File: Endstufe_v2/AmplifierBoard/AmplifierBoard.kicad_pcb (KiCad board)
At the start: 4 copper layers, 125 x 90 mm, 120 parts, among them J1 Conn_01x01_Pin, J10 Conn_02x06_Top_Bottom, J11 B6B-XH-2(LF)(SN), J12 B6B-XH-2(LF)(SN), J13 Conn_01x02_Pin, J14 Conn_01x02_Pin, J15 Conn_01x02_Pin, J16 Conn_01x04, J17 Conn_01x02_Pin, J2 Conn_01x01_Pin, J3 banana connector, J4 banana connector, J5 banana connector, J6 banana connector, J7 banana connector, J8 banana connector, J9 ST-0322D00-071-1A2H, U1 TPA3126D2DADR, U2 TPA3126D2DADR, U3 NVTFWS014P04M8LTAG, U4 1SMA5927A

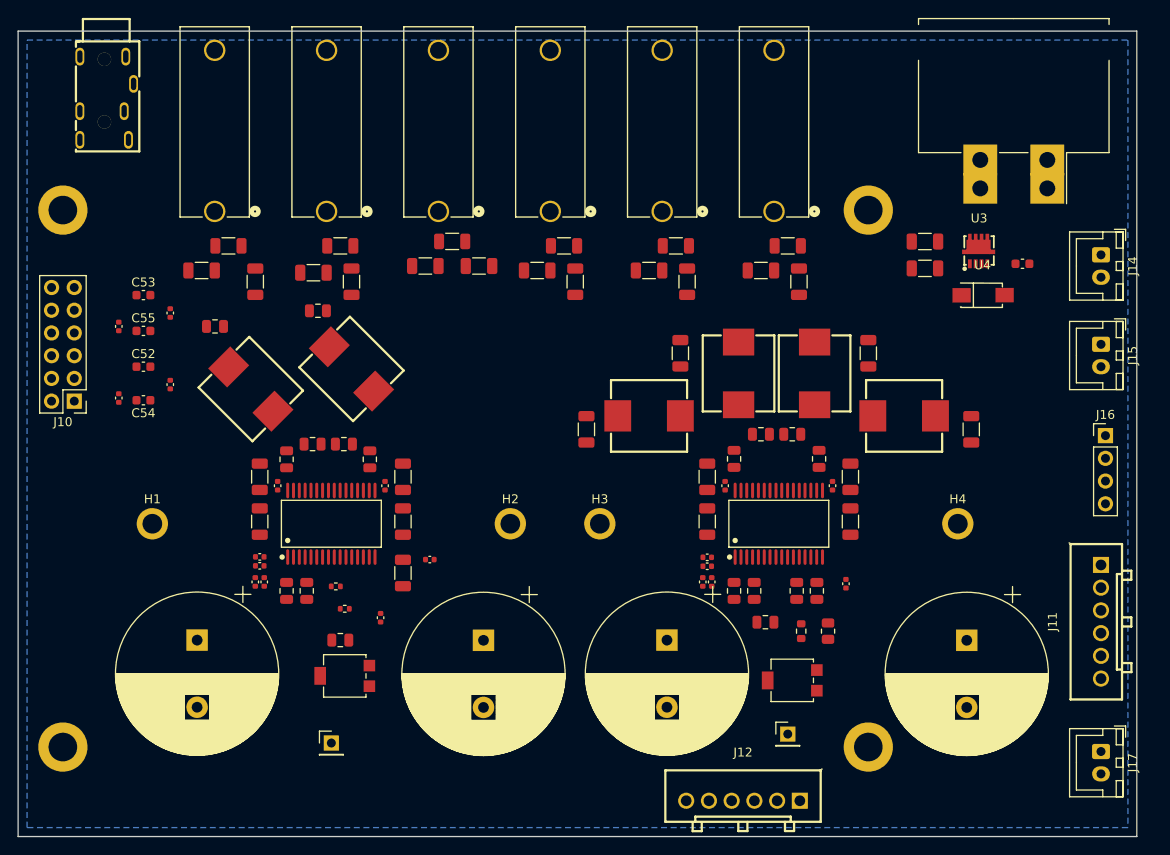
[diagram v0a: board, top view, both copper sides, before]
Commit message: Route Power and Audio Signals
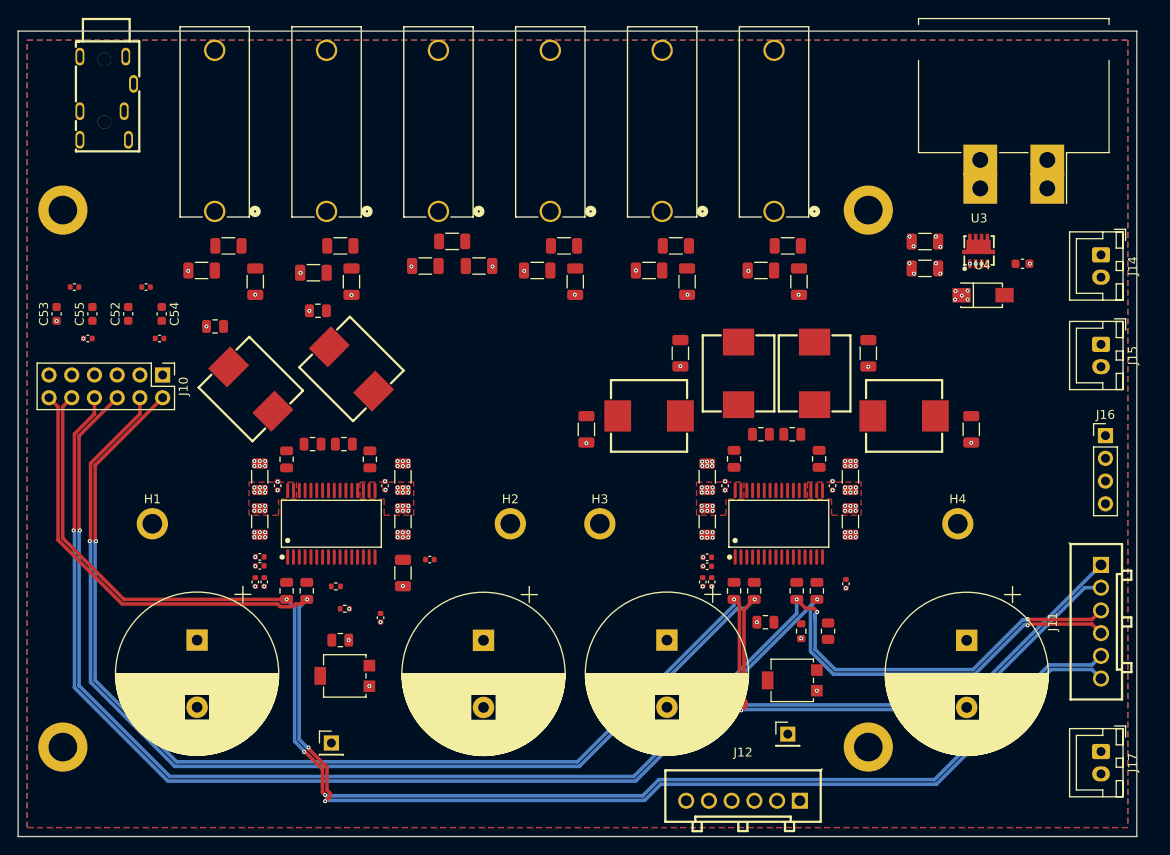
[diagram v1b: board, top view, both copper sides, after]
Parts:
- moved R18 11.2 mm to (149.3, 78.6), turned to 180 degrees
- moved R19 11.1 mm to (141.3, 78.6), turned to 180 degrees
- moved J10 10.3 mm to (151.2, 88.4), turned to -90 degrees
- moved C53 9.92 mm to (139.3, 81.6), turned to 90 degrees
- moved C54 9.87 mm to (151.1, 81.6), turned to -90 degrees
- moved R21 8.06 mm to (150.8, 84.3), turned to 180 degrees
- moved C52 6.14 mm to (147.3, 81.6), turned to 90 degrees
- moved C55 6.01 mm to (143.3, 81.6), turned to 90 degrees
- moved R20 3.70 mm to (142.8, 84.3), turned to 180 degrees
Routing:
- net /TPA3126D2/RINN: track 0.00 -> 179.1 mm, vias 0 -> 3
- net /TPA3126D2/RINP: track 0.00 -> 176.6 mm, vias 0 -> 3
- net /TPA3126D2/LINP: track 0.00 -> 171.0 mm, vias 0 -> 4
- net /TPA3126D2/LINN: track 0.00 -> 170.7 mm, vias 0 -> 3
- net /TPA3126D2/SINN: track 0.00 -> 165.6 mm, vias 0 -> 3
- net /TPA3126D2/SINP: track 0.00 -> 160.9 mm, vias 0 -> 3
- net GND: vias 0 -> 90
- net +24V: vias 0 -> 68
- added copper zone on F.Cu, net +24V
- added copper zone on F.Cu, net GND

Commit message: Route TPA3126D2 output signals
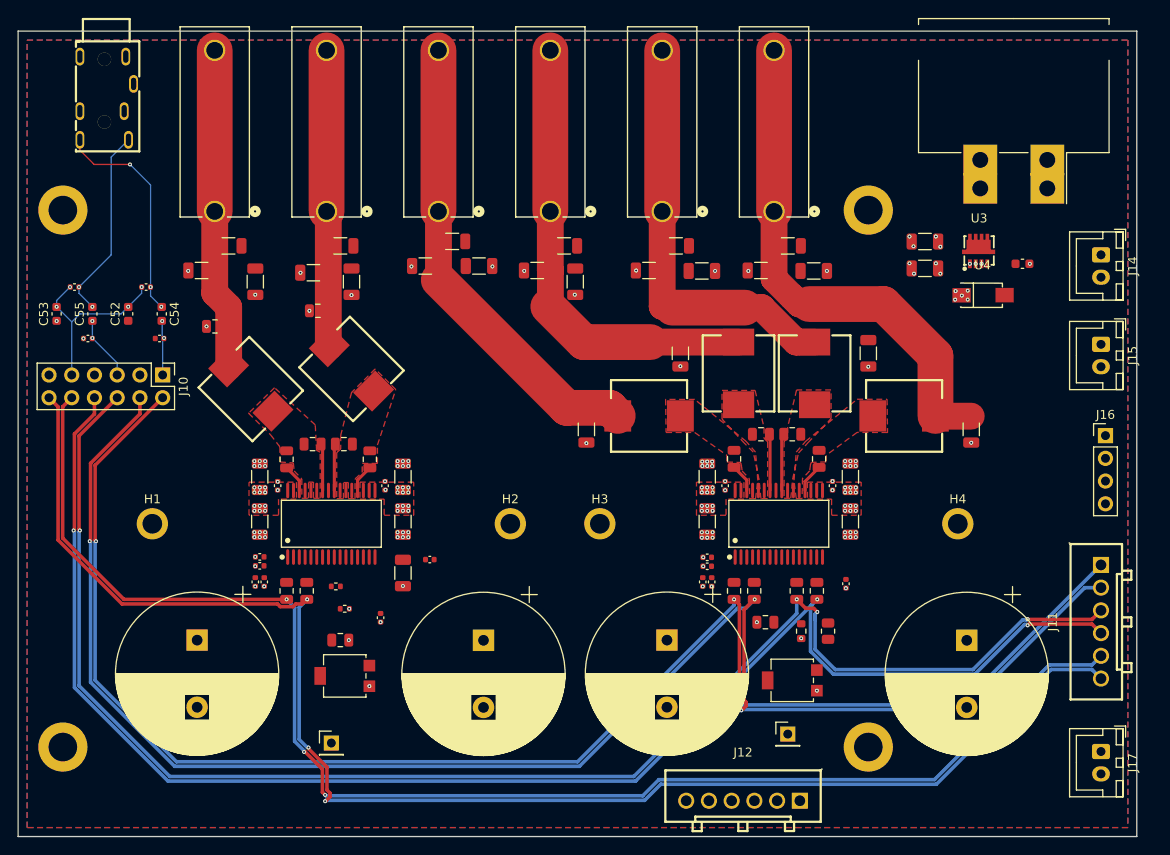
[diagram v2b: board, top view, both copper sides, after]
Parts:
- moved C48 2.04 mm to (211.4, 76.8), turned to 0 degrees
- moved C49 2.04 mm to (223.9, 76.8), turned to 180 degrees
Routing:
- net Net-(J6-Pin_1): track 0.00 -> 57.8 mm
- net Net-(J3-Pin_1): track 0.00 -> 52.0 mm
- net Net-(J4-Pin_1): track 0.00 -> 51.1 mm
- net Net-(J5-Pin_1): track 0.00 -> 47.3 mm
- net Net-(J7-Pin_1): track 0.00 -> 36.0 mm
- net Net-(J8-Pin_1): track 0.00 -> 33.3 mm
- net Net-(J9-AUDIO_R): track 0.00 -> 24.8 mm, vias 0 -> 3
- net Net-(J9-AUDIO_L): track 0.00 -> 21.6 mm, vias 0 -> 2
- net /SIN: track 0.00 -> 21.0 mm, vias 0 -> 4
- net /LIN: track 0.00 -> 7.17 mm, vias 0 -> 2
- net Net-(U1-BSPL): track 0.00 -> 6.37 mm
- net Net-(U1-BSNR): track 0.00 -> 6.31 mm
- net /RIN: track 0.00 -> 6.17 mm, vias 0 -> 2
- net Net-(U2-BSNR): track 0.00 -> 5.25 mm
- net Net-(U2-BSPL): track 0.00 -> 5.23 mm
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- added copper zone on F.Cu, net Net-(U1-OUTNL)
- added copper zone on F.Cu, net Net-(U1-OUTNR)
- added copper zone on F.Cu, net Net-(U1-OUTPL)
- added copper zone on F.Cu, net Net-(U1-OUTPR)
- added copper zone on F.Cu, net Net-(U2-OUTNL)
- added copper zone on F.Cu, net Net-(U2-OUTNR)

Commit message: Finish routing of amplifier board
Signals are now on layer 2, and layer 3 is 24V, layer 4 is GND.
This makes the outer layers solid GND without many heat flow obstacles
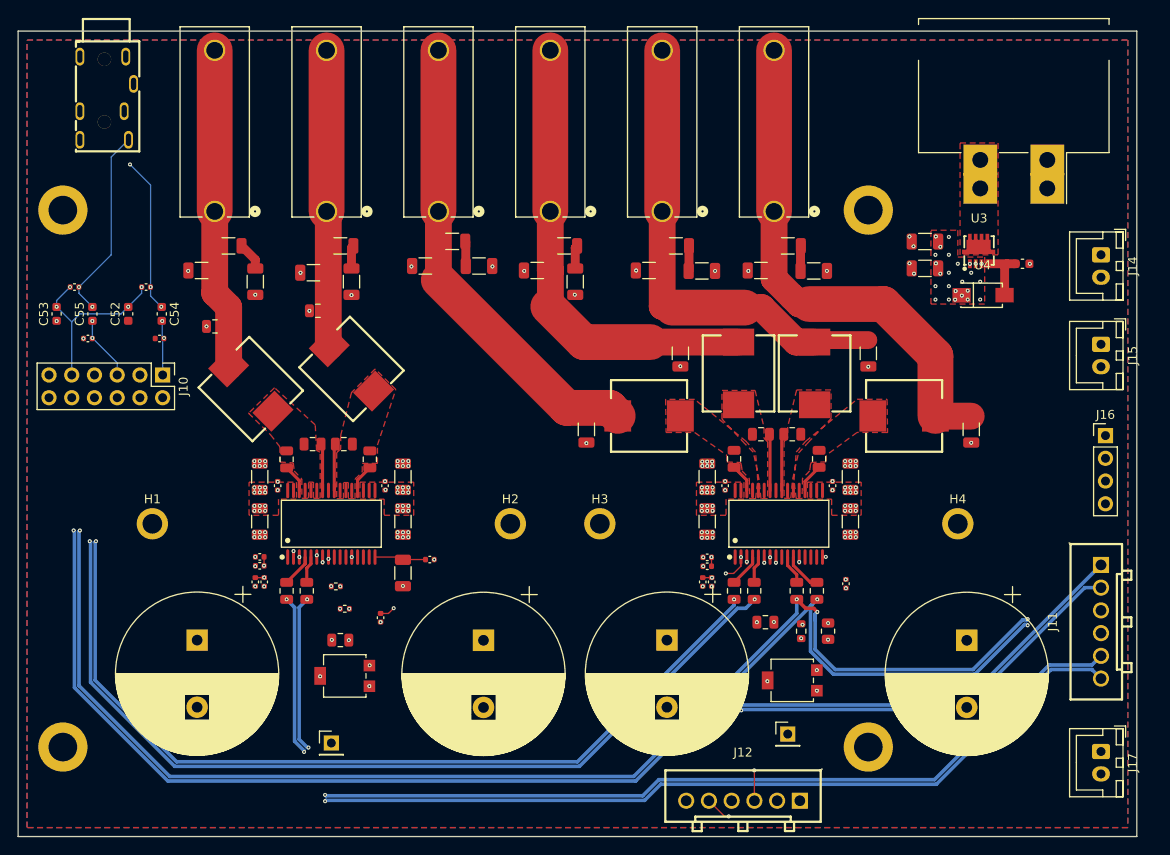
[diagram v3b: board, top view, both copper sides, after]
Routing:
- net /TPA3126D2/SDZB: track 0.00 -> 73.0 mm, vias 0 -> 2
- net /TPA3126D2/FAULTZB: track 0.00 -> 70.4 mm, vias 0 -> 2
- net /TPA3126D2/MUTEB: track 0.00 -> 51.0 mm, vias 0 -> 2
- net /TPA3126D2/SYNC: track 0.00 -> 46.9 mm, vias 0 -> 2
- net /TPA3126D2/MUTEA: track 0.00 -> 46.3 mm, vias 0 -> 3
- net /TPA3126D2/SDZA: track 0.00 -> 36.5 mm, vias 0 -> 3
- net /TPA3126D2/FAULTZA: track 0.00 -> 33.4 mm, vias 0 -> 3
- net Net-(J2-Pin_1): track 0.00 -> 21.6 mm, vias 0 -> 2
- net Net-(J1-Pin_1): track 0.00 -> 20.2 mm, vias 0 -> 2
- net Net-(U1-GVDD): track 0.00 -> 17.5 mm, vias 0 -> 4
- net Net-(U2-GVDD): track 0.00 -> 14.7 mm, vias 0 -> 4
- net Net-(U1-GAIN_SLV): track 0.00 -> 11.1 mm, vias 0 -> 3
- net Net-(U3-G): track 0.00 -> 6.58 mm
- net Net-(U2-GAIN_SLV): track 0.00 -> 6.21 mm, vias 0 -> 3
- net Net-(J5-Pin_1): track 47.3 -> 53.4 mm
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- added copper zone on In2.Cu, net +24V
- added copper zone on B.Cu, net GND
- added copper zone on F.Cu, net Net-(J13-Pin_2)
- removed copper zone on B.Cu, net +24V

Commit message: Make boards compliant with JLCPCB
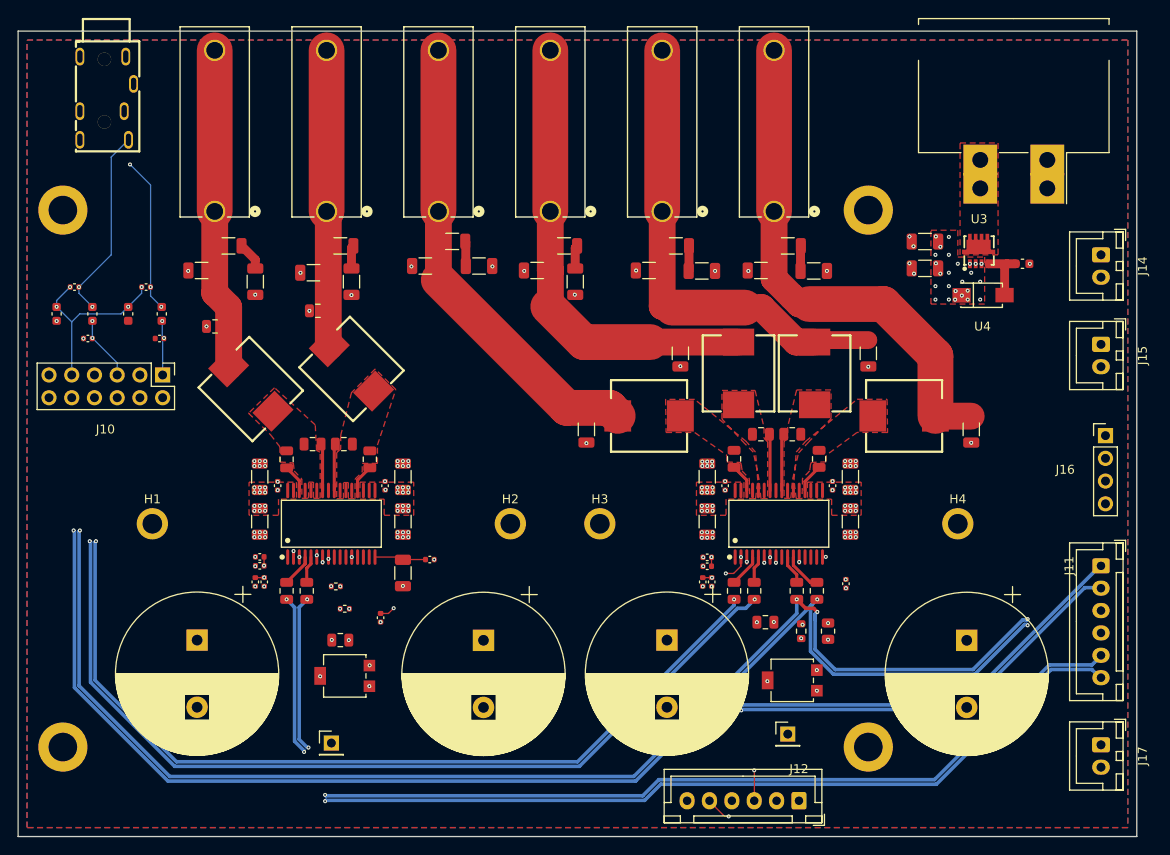
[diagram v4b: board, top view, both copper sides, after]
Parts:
- J10: value Conn_02x06_Top_Bottom -> DNP
- J11, J12: footprint Endstufe:CONN-TH_B6B-XH-2-LF-SN -> Endstufe:JST_XH_B6B-XH-A_1x06_P2.50mm_Vertical
- J13: value Conn_01x02_Pin -> DNP
- J14, J15, J17: footprint Connector_JST:JST_XH_B2B-XH-A_1x02_P2.50mm_Vertical -> Endstufe:JST_XH_B2B-XH-A_1x02_P2.50mm_Vertical
- J16: value Conn_01x04 -> DNP
- moved J14 1.25 mm to (256.0, 76.2), turned to 90 degrees
- moved J15 1.25 mm to (256.0, 86.2), turned to 90 degrees
- moved J17 0.50 mm to (256.0, 131.0), turned to 90 degrees

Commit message: Change unavailable parts to available ones, optimise silkscreen, do via stiching
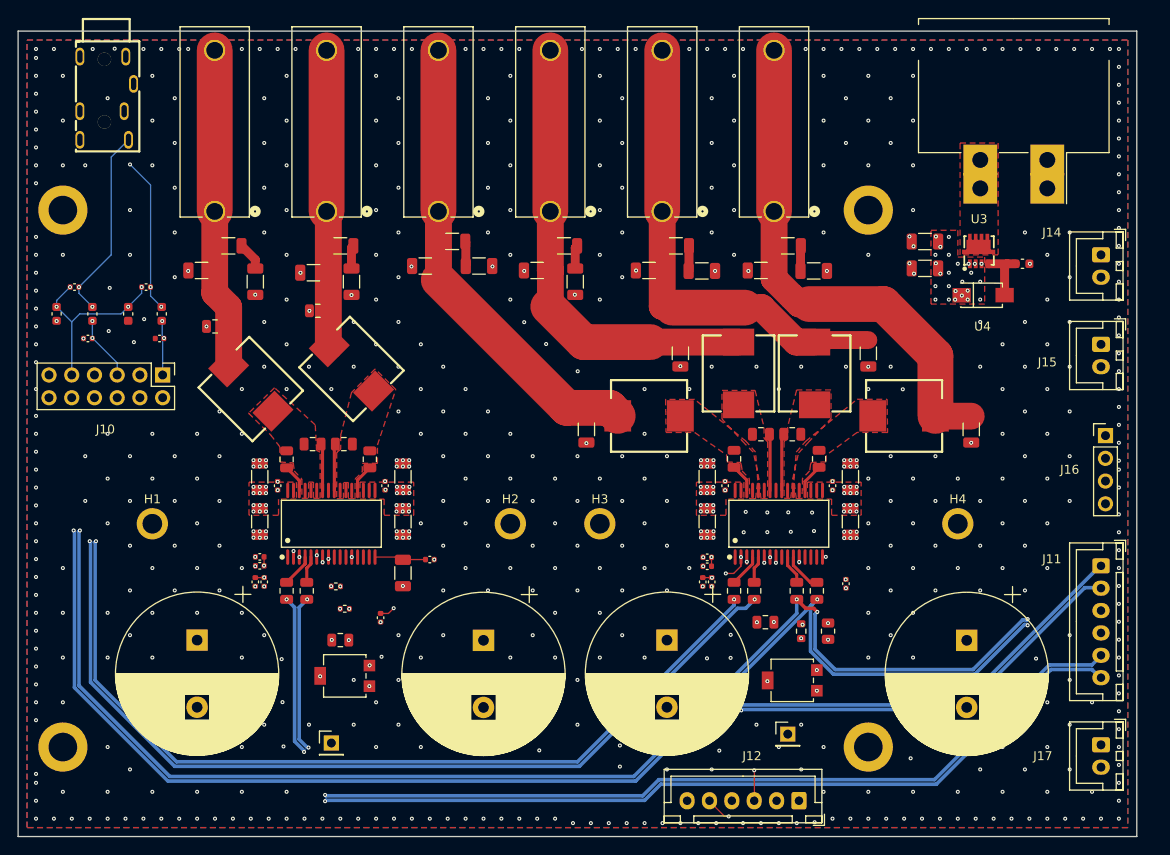
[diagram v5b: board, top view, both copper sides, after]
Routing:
- net /TPA3126D2/LINP: track 171.0 -> 170.4 mm
- net GND: vias 90 -> 644
